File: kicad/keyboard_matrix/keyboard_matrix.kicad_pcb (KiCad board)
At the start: 2 copper layers, 175.3 x 36.2 mm, 25 parts, among them J1 Conn_01x09, SW1 SPST, SW10 SPST, SW11 SPST, SW12 SPST, SW13 SPST, SW14 SPST, SW15 SPST, SW16 SPST, SW17 SPST, SW18 SPST, SW19 SPST, SW2 SPST, SW20 SPST, SW3 SPST, SW4 SPST, SW5 SPST, SW6 SPST, SW7 SPST, SW8 SPST, SW9 SPST

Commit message: amend
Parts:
- removed the   at (185.6, 78.7)
- removed the   at (130.0, 78.7)
- removed the   at (241.3, 78.7)
- added  : 3.2mm, MountingHole:MountingHole_3.2mm_M3, F.Cu at (186.0, 78.7)
- added  : 3.2mm, MountingHole:MountingHole_3.2mm_M3, F.Cu at (130.1, 78.7)
- added  : 3.2mm, MountingHole:MountingHole_3.2mm_M3, F.Cu at (241.9, 78.7)
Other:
- board text added: "REV _A"
- board text removed: "rev xyz123"

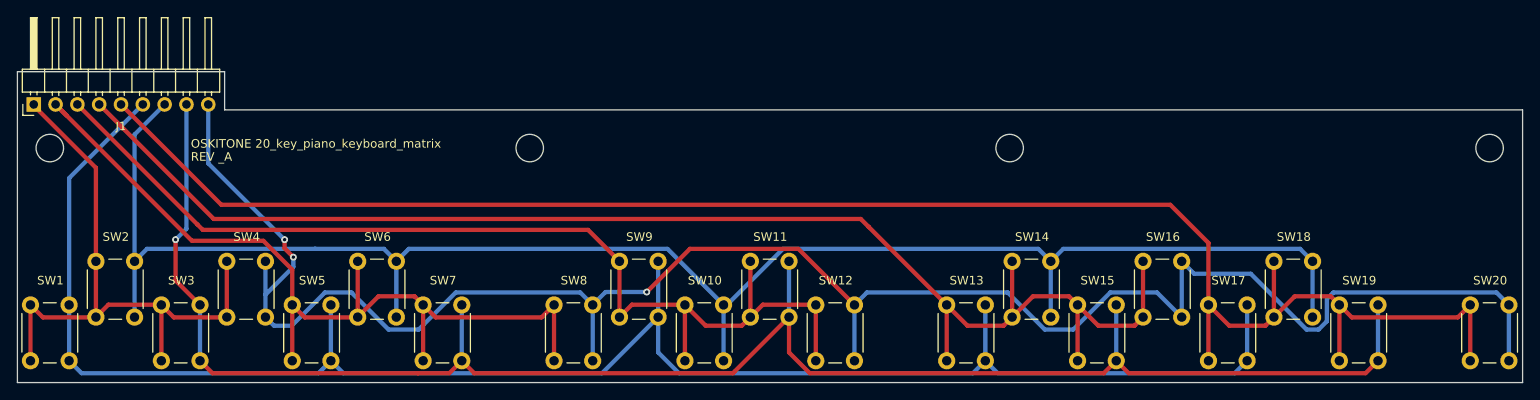
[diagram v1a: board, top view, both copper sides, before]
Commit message: Move header to middle
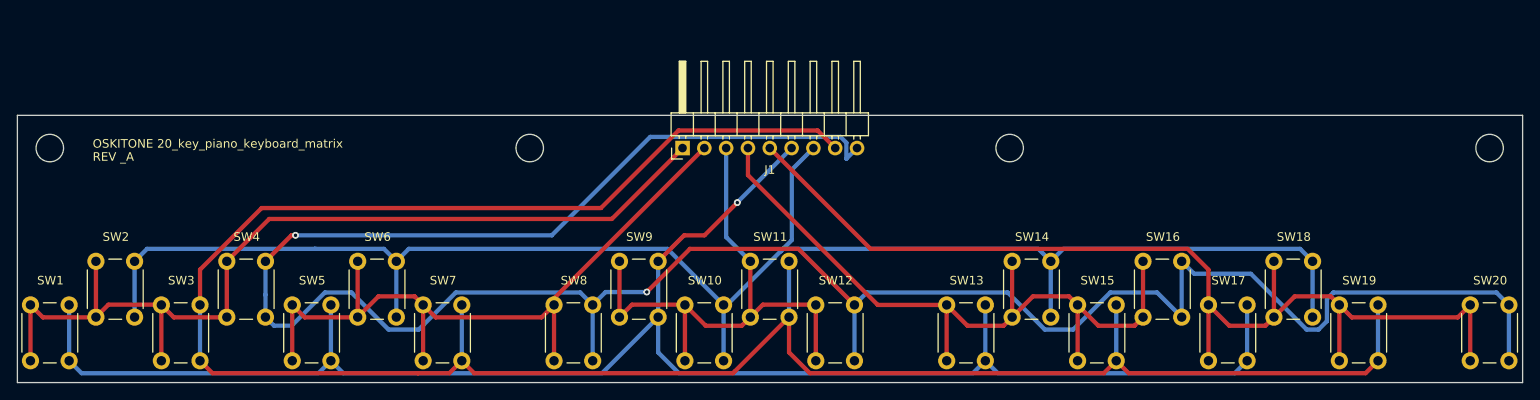
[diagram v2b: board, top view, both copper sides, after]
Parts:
- moved J1 75.7 mm to (147.9, 78.7)
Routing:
- net /C5: track 201.0 -> 121.6 mm
- net /C4: track 161.6 -> 85.7 mm
- net /R3: track 206.2 -> 266.8 mm, vias 1 -> 0
- net /C3: track 122.2 -> 65.9 mm
- net /R4: track 229.1 -> 279.0 mm, vias 3 -> 2
- net /C1: track 72.0 -> 109.2 mm
- net /C2: track 101.2 -> 85.2 mm
- net /R2: track 198.5 -> 192.4 mm
- net /R1: track 208.0 -> 202.1 mm, vias 0 -> 1
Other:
- board size 175.3 x 36.2 mm -> 175.3 x 31.1 mm

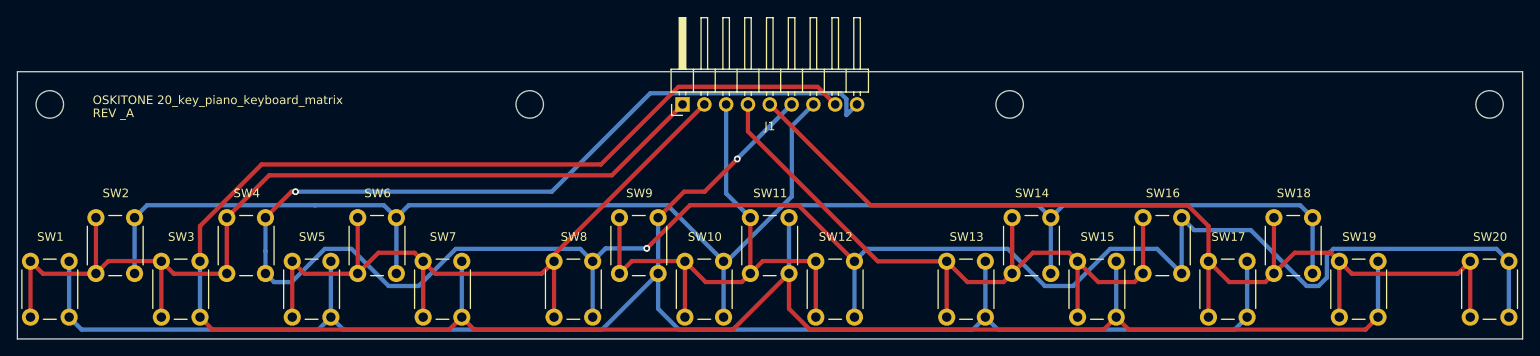
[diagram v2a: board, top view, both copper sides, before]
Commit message: Tighten mechanical advantage
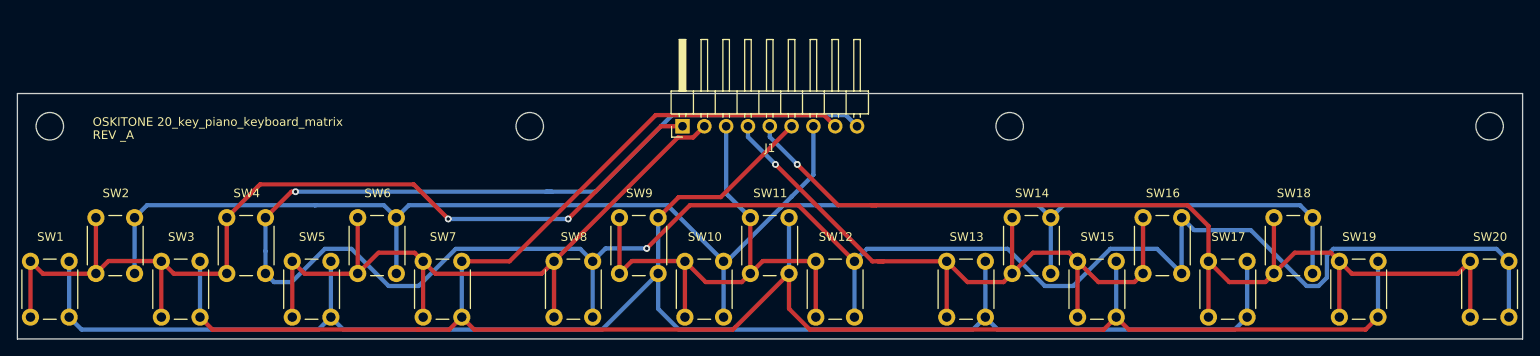
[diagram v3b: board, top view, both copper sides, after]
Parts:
- removed the   at (186.0, 78.7)
- removed the   at (130.1, 78.7)
- removed the   at (241.9, 78.7)
- added  : 3.2mm, MountingHole:MountingHole_3.2mm_M3, F.Cu at (186.0, 81.3)
- added  : 3.2mm, MountingHole:MountingHole_3.2mm_M3, F.Cu at (130.1, 81.3)
- added  : 3.2mm, MountingHole:MountingHole_3.2mm_M3, F.Cu at (241.9, 81.3)
- moved   2.54 mm to (74.3, 81.3)
- moved J1 2.54 mm to (147.9, 81.3)
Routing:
- net /R3: track 266.8 -> 232.3 mm
- net /C3: track 65.9 -> 63.3 mm
- net /R4: track 279.0 -> 276.5 mm
- net /R2: track 192.4 -> 189.9 mm
- net /C1: track 109.2 -> 111.5 mm, vias 0 -> 2
- net /C4: track 85.7 -> 84.1 mm, vias 0 -> 1
- net /C2: track 85.2 -> 83.7 mm
- net /R1: track 202.1 -> 201.0 mm, vias 1 -> 0
- net /C5: track 121.6 -> 121.9 mm, vias 0 -> 1
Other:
- board size 175.3 x 31.1 mm -> 175.3 x 28.6 mm

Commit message: Reorient matrix to 0,0
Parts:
- removed the   at (186.0, 81.3)
- removed the   at (130.1, 81.3)
- removed the   at (241.9, 81.3)
- added  : 3.2mm, MountingHole:MountingHole_3.2mm_M3, F.Cu at (115.5, -24.8)
- added  : 3.2mm, MountingHole:MountingHole_3.2mm_M3, F.Cu at (59.7, -24.8)
- added  : 3.2mm, MountingHole:MountingHole_3.2mm_M3, F.Cu at (171.4, -24.8)
- moved   127.3 mm to (3.77, -24.8)
- moved J1 127.3 mm to (77.4, -24.8)
- moved SW1 127.3 mm to (1.52, -2.54)
- moved SW10 127.3 mm to (77.7, -2.54)
- moved SW11 127.3 mm to (85.3, -7.62)
- moved SW12 127.3 mm to (93.0, -2.54)
- moved SW13 127.3 mm to (108.2, -2.54)
- moved SW14 127.3 mm to (115.8, -7.62)
- moved SW15 127.3 mm to (123.4, -2.54)
- moved SW16 127.3 mm to (131.1, -7.62)
- moved SW17 127.3 mm to (138.7, -2.54)
- moved SW18 127.3 mm to (146.3, -7.62)
- moved SW19 127.3 mm to (153.9, -2.54)
- moved SW2 127.3 mm to (9.14, -7.62)
- moved SW20 127.3 mm to (169.2, -2.54)
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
